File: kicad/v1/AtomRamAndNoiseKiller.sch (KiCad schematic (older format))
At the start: 23 parts, among them J1 Conn_01x10, J2 Conn_01x10, J3 Conn_01x03, J4 Conn_01x09, J5 Conn_01x09, J6 Conn_01x03, J7 Conn_01x02, J8 Conn_01x01, U1 74LS123, U2 74LS00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

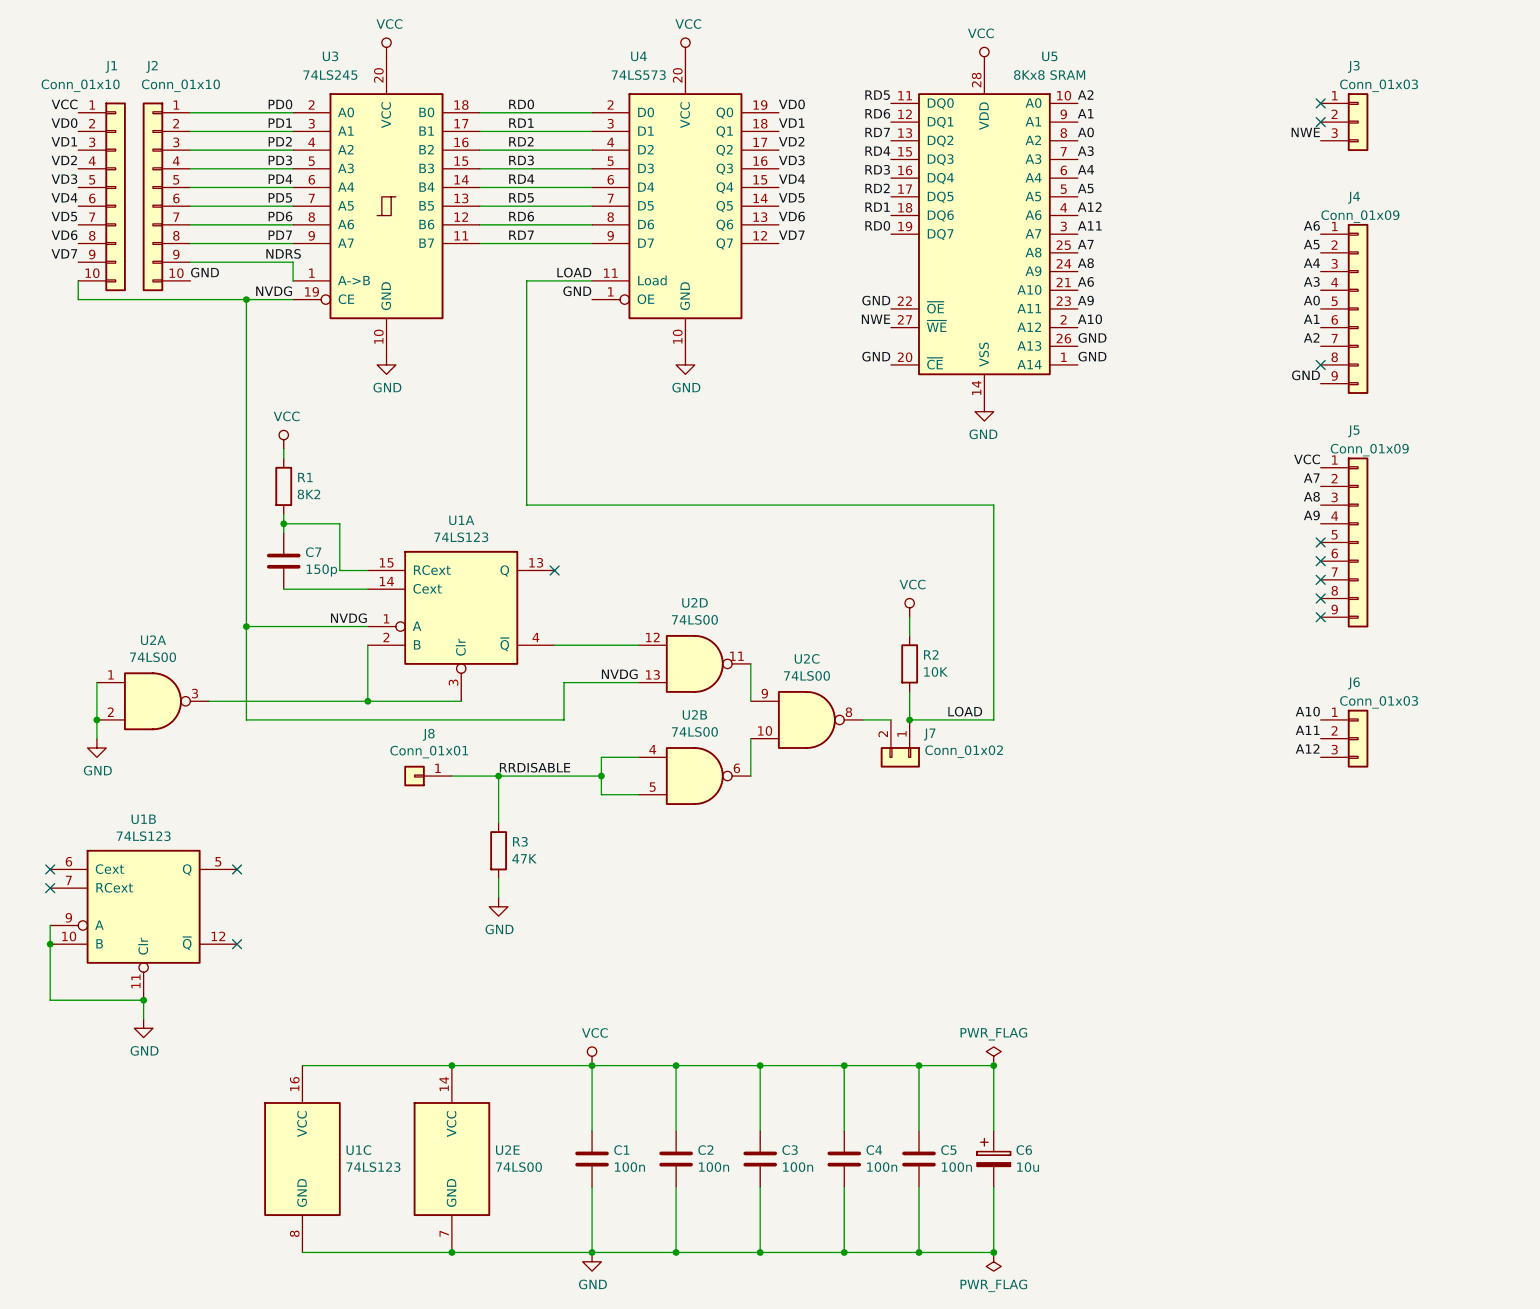
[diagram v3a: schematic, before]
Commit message: Switched to HCT parts (cheaper)
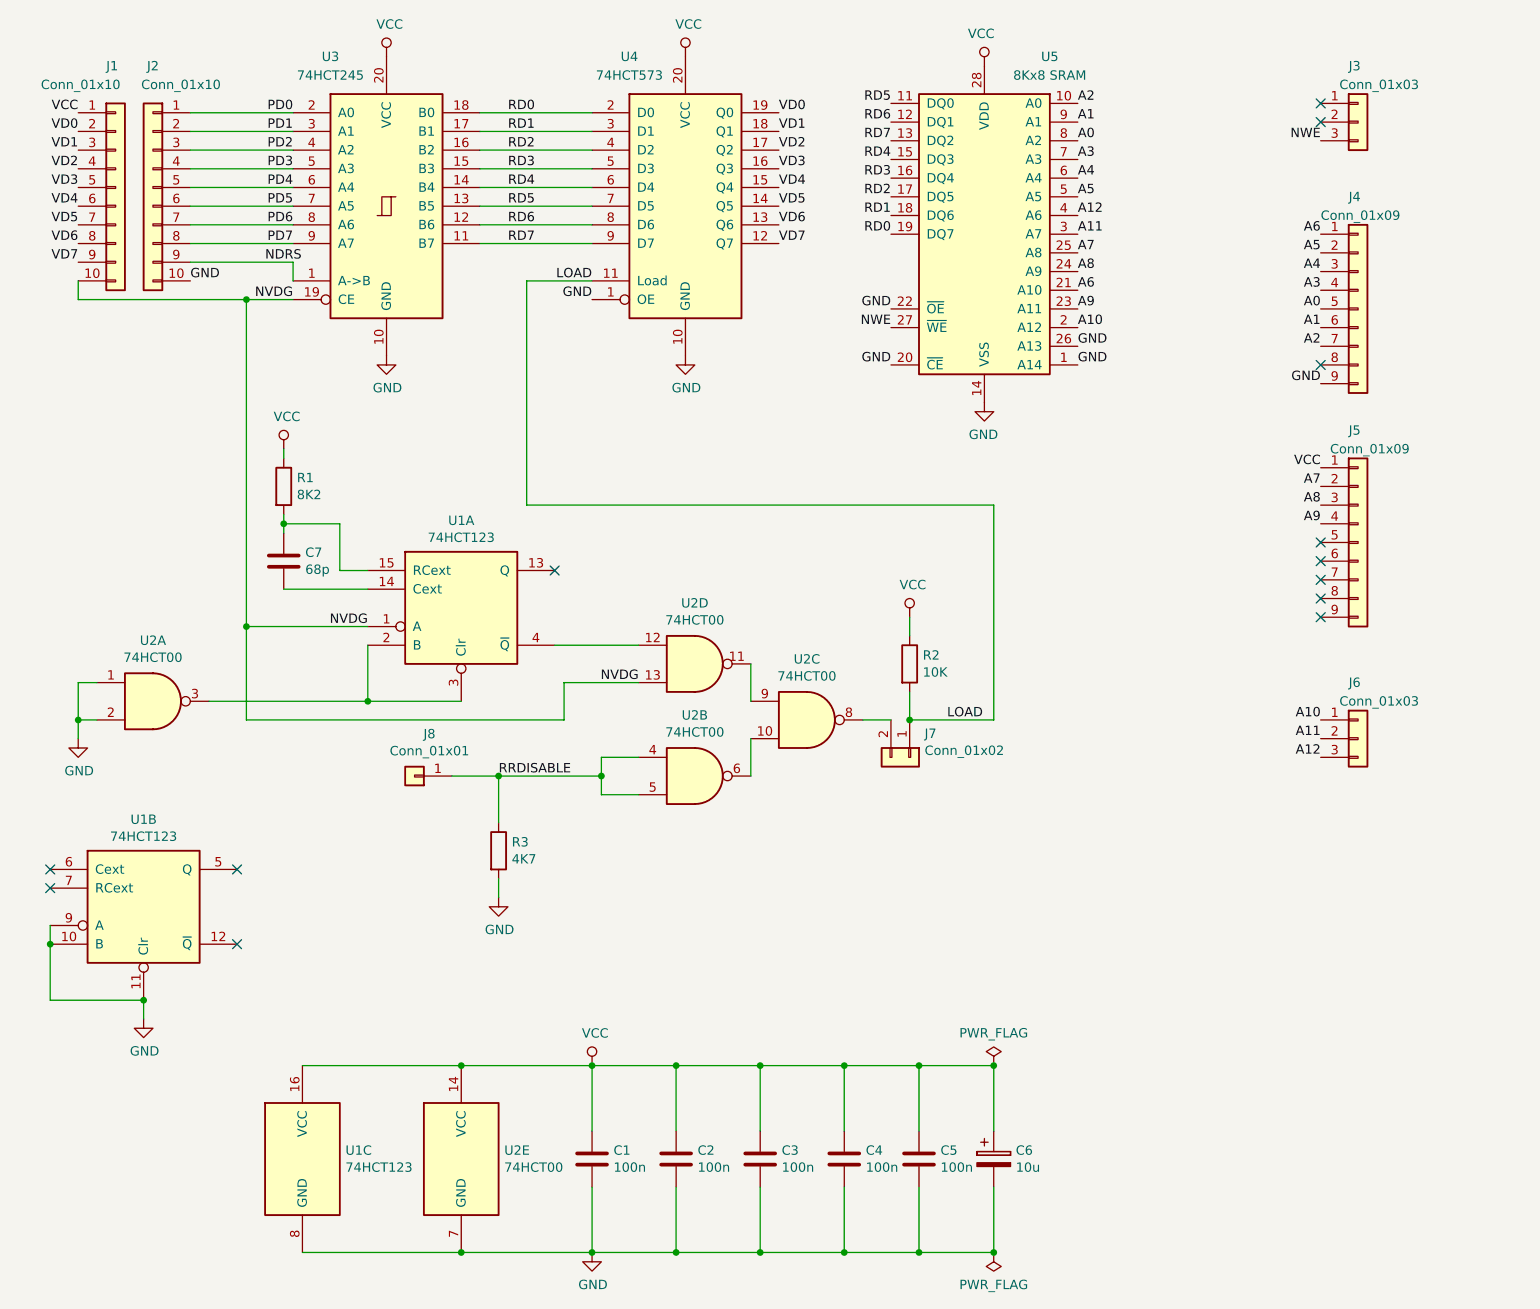
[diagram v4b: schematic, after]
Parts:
- removed U1: 74LS123, Package_DIP:DIP-16_W7.62mm_Socket, symbol 74xx:74LS123
- removed U2: 74LS00, Package_DIP:DIP-14_W7.62mm_Socket, symbol 74xx:74LS00
- added U1: 74HCT123, Package_DIP:DIP-16_W7.62mm_Socket, symbol 74xx:74HCT123
- added U2: 74HCT00, Package_DIP:DIP-14_W7.62mm_Socket, symbol 74xx:74HCT00
- C7: value 150p -> 68p
- R3: value 47K -> 4K7
- U3: value 74LS245 -> 74HCT245
- U4: value 74LS573 -> 74HCT573
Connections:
- net GND: now also U1.10 (B), U1.11 (Clr), U1.8 (GND), U1.9 (A), U2.1, U2.2, U2.7 (GND)
- net NVDG: now also U1.1 (A), U2.13
- net RRDISABLE: now also U2.4, U2.5
- net VCC: now also U1.16 (VCC), U2.14 (VCC)
- net at C7.2: now also U1.14 (Cext)
- net at C7.1, R1.2: now also U1.15 (RCext)
- net at J7.2 (Pin_2): now also U2.8
- new net: U1.2 (B), U1.3 (Clr), U2.3
- new net: U1.4 (~Q), U2.12
- new net: U2.10, U2.6
- new net: U2.11, U2.9
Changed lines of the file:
@@
 U 1 1 5CB31091
 P 4450 1850
-F 0 "U4" H 4200 2650 50  0000 C CNN
-F 1 "74LS573" H 4200 2550 50  0000 C CNN
+F 0 "U4" H 4150 2650 50  0000 C CNN
+F 1 "74HCT573" H 4150 2550 50  0000 C CNN
 F 2 "Package_DIP:DIP-20_W7.62mm_Socket" H 4450 1850 50  0001 C CNN
 F 3 "74xx/74hc573.pdf" H 4450 1850 50  0001 C CNN
@@
 P 2850 1850
 F 0 "U3" H 2550 2650 50  0000 C CNN
-F 1 "74LS245" H 2550 2550 50  0000 C CNN
+F 1 "74HCT245" H 2550 2550 50  0000 C CNN
 F 2 "Package_DIP:DIP-20_W7.62mm_Socket" H 2850 1850 50  0001 C CNN
 F 3 "http://www.ti.com/lit/gpn/sn74LS245" H 2850 1850 50  0001 C CNN
 	1    2850 1850
-	1    0    0    -1
-$EndComp
-$Comp
-L 74xx:74LS00 U2
-U 4 1 5CB3125F
-P 4500 4300
-F 0 "U2" H 4500 4625 50  0000 C CNN
-F 1 "74LS00" H 4500 4534 50  0000 C CNN
-F 2 "Package_DIP:DIP-14_W7.62mm_Socket" H 4500 4300 50  0001 C CNN
-F 3 "http://www.ti.com/lit/gpn/sn74ls00" H 4500 4300 50  0001 C CNN
-	4    4500 4300
-	1    0    0    -1
-$EndComp
-$Comp
-L 74xx:74LS123 U1
-U 1 1 5CB31357
-P 3250 4000
-F 0 "U1" H 3250 4467 50  0000 C CNN
-F 1 "74LS123" H 3250 4376 50  0000 C CNN
-F 2 "Package_DIP:DIP-16_W7.62mm_Socket" H 3250 4000 50  0001 C CNN
-F 3 "http://www.ti.com/lit/gpn/sn74LS123" H 3250 4000 50  0001 C CNN
-	1    3250 4000
 	1    0    0    -1
 $EndComp
@@
 P 2300 3750
 F 0 "C7" H 2415 3796 50  0000 L CNN
-F 1 "150p" H 2415 3705 50  0000 L CNN
+F 1 "68p" H 2415 3705 50  0000 L CNN
 F 2 "Capacitor_THT:C_Rect_L7.0mm_W2.0mm_P5.00mm" H 2338 3600 50  0001 C CNN
 F 3 "~" H 2300 3750 50  0001 C CNN
@@
 Text Label 5550 1500 2    50   ~ 0
 RD7
-$Comp
-L 74xx:74LS00 U2
-U 2 1 5CB33DE5
-P 4500 4900
-F 0 "U2" H 4500 5225 50  0000 C CNN
-F 1 "74LS00" H 4500 5134 50  0000 C CNN
-F 2 "Package_DIP:DIP-14_W7.62mm_Socket" H 4500 4900 50  0001 C CNN
-F 3 "http://www.ti.com/lit/gpn/sn74ls00" H 4500 4900 50  0001 C CNN
-	2    4500 4900
-	1    0    0    -1
-$EndComp
-$Comp
-L 74xx:74LS00 U2
-U 5 1 5CB33E8A
-P 3200 6950
-F 0 "U2" H 3430 6996 50  0000 L CNN
-F 1 "74LS00" H 3430 6905 50  0000 L CNN
-F 2 "Package_DIP:DIP-14_W7.62mm_Socket" H 3200 6950 50  0001 C CNN
-F 3 "http://www.ti.com/lit/gpn/sn74ls00" H 3200 6950 50  0001 C CNN
-	5    3200 6950
-	1    0    0    -1
-$EndComp
-$Comp
-L 74xx:74LS123 U1
-U 2 1 5CB33F3B
-P 1550 5600
-F 0 "U1" H 1550 6067 50  0000 C CNN
-F 1 "74LS123" H 1550 5976 50  0000 C CNN
-F 2 "Package_DIP:DIP-16_W7.62mm_Socket" H 1550 5600 50  0001 C CNN
-F 3 "http://www.ti.com/lit/gpn/sn74LS123" H 1550 5600 50  0001 C CNN
-	2    1550 5600
-	1    0    0    -1
-$EndComp
-$Comp
-L 74xx:74LS123 U1
-U 3 1 5CB34024
-P 2400 6950
-F 0 "U1" H 2630 6996 50  0000 L CNN
-F 1 "74LS123" H 2630 6905 50  0000 L CNN
-F 2 "Package_DIP:DIP-16_W7.62mm_Socket" H 2400 6950 50  0001 C CNN
-F 3 "http://www.ti.com/lit/gpn/sn74LS123" H 2400 6950 50  0001 C CNN
-	3    2400 6950
-	1    0    0    -1
-$EndComp
-Wire Wire Line
-	2400 7450 3200 7450
 Wire Wire Line
 	6100 7450 6100 7100
-Connection ~ 3200 7450
-Wire Wire Line
-	3200 7450 3950 7450
 Wire Wire Line
 	5700 7100 5700 7450
@@
 	6100 6450 6100 6800
 Wire Wire Line
-	2400 6450 3200 6450
-Connection ~ 3200 6450
-Wire Wire Line
 	3950 6800 3950 6450
 Connection ~ 3950 6450
-Wire Wire Line
-	3950 6450 3200 6450
 Wire Wire Line
 	4400 6800 4400 6450
@@
 Text Label 4200 4400 2    50   ~ 0
 NVDG
-$Comp
-L 74xx:74LS00 U2
-U 3 1 5CB46B81
-P 5100 4600
-F 0 "U2" H 5100 4925 50  0000 C CNN
-F 1 "74LS00" H 5100 4834 50  0000 C CNN
-F 2 "Package_DIP:DIP-14_W7.62mm_Socket" H 5100 4600 50  0001 C CNN
-F 3 "http://www.ti.com/lit/gpn/sn74ls00" H 5100 4600 50  0001 C CNN
-	3    5100 4600
-	1    0    0    -1
-$EndComp
 Wire Wire Line
 	4800 4300 4800 4500
@@
 P 3450 5300
 F 0 "R3" H 3520 5346 50  0000 L CNN
-F 1 "47K" H 3520 5255 50  0000 L CNN
+F 1 "4K7" H 3520 5255 50  0000 L CNN
 F 2 "Resistor_THT:R_Axial_DIN0207_L6.3mm_D2.5mm_P10.16mm_Horizontal" V 3380 5300 50  0001 C CNN
 F 3 "~" H 3450 5300 50  0001 C CNN
@@
 Text Label 3450 4900 0    50   ~ 0
 RRDISABLE
-$Comp
-L 74xx:74LS00 U2
-U 1 1 5CB560A6
-P 1600 4500
-F 0 "U2" H 1600 4825 50  0000 C CNN
-F 1 "74LS00" H 1600 4734 50  0000 C CNN
-F 2 "Package_DIP:DIP-14_W7.62mm_Socket" H 1600 4500 50  0001 C CNN
-F 3 "http://www.ti.com/lit/gpn/sn74ls00" H 1600 4500 50  0001 C CNN
-	1    1600 4500
-	1    0    0    -1
-$EndComp
 Wire Wire Line
 	1900 4500 2750 4500
-Wire Wire Line
-	1300 4400 1300 4600
-Wire Wire Line
-	1300 4600 1300 4700
-Connection ~ 1300 4600
 $Comp
 L power:GND #PWR01
 U 1 1 5CB5EA3A
-P 1300 4700
-F 0 "#PWR01" H 1300 4450 50  0001 C CNN
-F 1 "GND" H 1305 4527 50  0000 C CNN
-F 2 "" H 1300 4700 50  0001 C CNN
-F 3 "" H 1300 4700 50  0001 C CNN
-	1    1300 4700
-	1    0    0    -1
-$EndComp
-Wire Wire Line
-	1050 5700 1050 5800
+P 1200 4700
+F 0 "#PWR01" H 1200 4450 50  0001 C CNN
+F 1 "GND" H 1205 4527 50  0000 C CNN
+F 2 "" H 1200 4700 50  0001 C CNN
+F 3 "" H 1200 4700 50  0001 C CNN
+	1    1200 4700
+	1    0    0    -1
+$EndComp
 Wire Wire Line
 	1050 6100 1550 6100
-Connection ~ 1050 5800
-Wire Wire Line
-	1050 5800 1050 6100
 Wire Wire Line
 	1550 6100 1550 6200
-Connection ~ 1550 6100
 $Comp
 L power:GND #PWR02
@@
 Text Label 1200 1450 2    50   ~ 0
 VD0
+$Comp
+L 74xx:74HCT123 U1
+U 1 1 5CB75C76
+P 3250 4000
+F 0 "U1" H 3250 4467 50  0000 C CNN
+F 1 "74HCT123" H 3250 4376 50  0000 C CNN
+F 2 "Package_DIP:DIP-16_W7.62mm_Socket" H 3250 4000 50  0001 C CNN
+F 3 "https://assets.nexperia.com/documents/data-sheet/74HC_HCT123.pdf" H 3250 4000 50  0001 C CNN
+	1    3250 4000
+	1    0    0    -1
+$EndComp
+$Comp
+L 74xx:74HCT123 U1
+U 2 1 5CB75D20
+P 1550 5600
+F 0 "U1" H 1550 6067 50  0000 C CNN
+F 1 "74HCT123" H 1550 5976 50  0000 C CNN
+F 2 "Package_DIP:DIP-16_W7.62mm_Socket" H 1550 5600 50  0001 C CNN
+F 3 "https://assets.nexperia.com/documents/data-sheet/74HC_HCT123.pdf" H 1550 5600 50  0001 C CNN
+	2    1550 5600
+	1    0    0    -1
+$EndComp
+Wire Wire Line
+	1050 5800 1050 6100
+Connection ~ 1550 6100
+Wire Wire Line
+	1050 5700 1050 5800
+Connection ~ 1050 5800
+$Comp
+L 74xx:74HCT00 U2
+U 1 1 5CB785EC
+P 1600 4500
+F 0 "U2" H 1600 4825 50  0000 C CNN
+F 1 "74HCT00" H 1600 4734 50  0000 C CNN
+F 2 "Package_DIP:DIP-14_W7.62mm_Socket" H 1600 4500 50  0001 C CNN
+F 3 "http://www.ti.com/lit/gpn/sn74hct00" H 1600 4500 50  0001 C CNN
+	1    1600 4500
+	1    0    0    -1
+$EndComp
+Wire Wire Line
+	1300 4600 1200 4600
+$Comp
+L 74xx:74HCT00 U2
+U 2 1 5CB7868E
+P 4500 4900
+F 0 "U2" H 4500 5225 50  0000 C CNN
+F 1 "74HCT00" H 4500 5134 50  0000 C CNN
+F 2 "Package_DIP:DIP-14_W7.62mm_Socket" H 4500 4900 50  0001 C CNN
+F 3 "http://www.ti.com/lit/gpn/sn74hct00" H 4500 4900 50  0001 C CNN
+	2    4500 4900
+	1    0    0    -1
+$EndComp
+$Comp
+L 74xx:74HCT00 U2
+U 3 1 5CB78730
+P 5100 4600
+F 0 "U2" H 5100 4925 50  0000 C CNN
+F 1 "74HCT00" H 5100 4834 50  0000 C CNN
+F 2 "Package_DIP:DIP-14_W7.62mm_Socket" H 5100 4600 50  0001 C CNN
+F 3 "http://www.ti.com/lit/gpn/sn74hct00" H 5100 4600 50  0001 C CNN
+	3    5100 4600
+	1    0    0    -1
+$EndComp
+$Comp
+L 74xx:74HCT00 U2
+U 4 1 5CB7878C
+P 4500 4300
+F 0 "U2" H 4500 4625 50  0000 C CNN
+F 1 "74HCT00" H 4500 4534 50  0000 C CNN
+F 2 "Package_DIP:DIP-14_W7.62mm_Socket" H 4500 4300 50  0001 C CNN
+F 3 "http://www.ti.com/lit/gpn/sn74hct00" H 4500 4300 50  0001 C CNN
+	4    4500 4300
+	1    0    0    -1
+$EndComp
+Wire Wire Line
+	2400 6450 3250 6450
+Wire Wire Line
+	2400 7450 3250 7450
+$Comp
+L 74xx:74HCT123 U1
+U 3 1 5CB788BB
+P 2400 6950
+F 0 "U1" H 2630 6996 50  0000 L CNN
+F 1 "74HCT123" H 2630 6905 50  0000 L CNN
+F 2 "Package_DIP:DIP-16_W7.62mm_Socket" H 2400 6950 50  0001 C CNN
+F 3 "https://assets.nexperia.com/documents/data-sheet/74HC_HCT123.pdf" H 2400 6950 50  0001 C CNN
+	3    2400 6950
+	1    0    0    -1
+$EndComp
+$Comp
+L 74xx:74HCT00 U2
+U 5 1 5CB78A47
+P 3250 6950
+F 0 "U2" H 3480 6996 50  0000 L CNN
+F 1 "74HCT00" H 3480 6905 50  0000 L CNN
+F 2 "Package_DIP:DIP-14_W7.62mm_Socket" H 3250 6950 50  0001 C CNN
+F 3 "http://www.ti.com/lit/gpn/sn74hct00" H 3250 6950 50  0001 C CNN
+	5    3250 6950
+	1    0    0    -1
+$EndComp
+Connection ~ 3250 6450
+Wire Wire Line
+	3250 6450 3950 6450
+Connection ~ 3250 7450
+Wire Wire Line
+	3250 7450 3950 7450
+Wire Wire Line
+	1200 4700 1200 4600
+Wire Wire Line
+	1200 4600 1200 4400
+Wire Wire Line
+	1200 4400 1300 4400
+Connection ~ 1200 4600
 $EndSCHEMATC
